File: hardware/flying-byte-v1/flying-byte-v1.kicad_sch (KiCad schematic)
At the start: 44 parts, among them J1 Conn_Coaxial, J2 Conn_ARM_SWD_TagConnect_TC2030, J3 USB_C_Receptacle_USB2.0, J4 Conn_01x04, SW1 SW_Push, U1 STM32WB55CEU6, U2 USBLC6-2SC6_MOD, U3 MIC5365-3.3YD5, X1 32MHz, X2 32kHz768

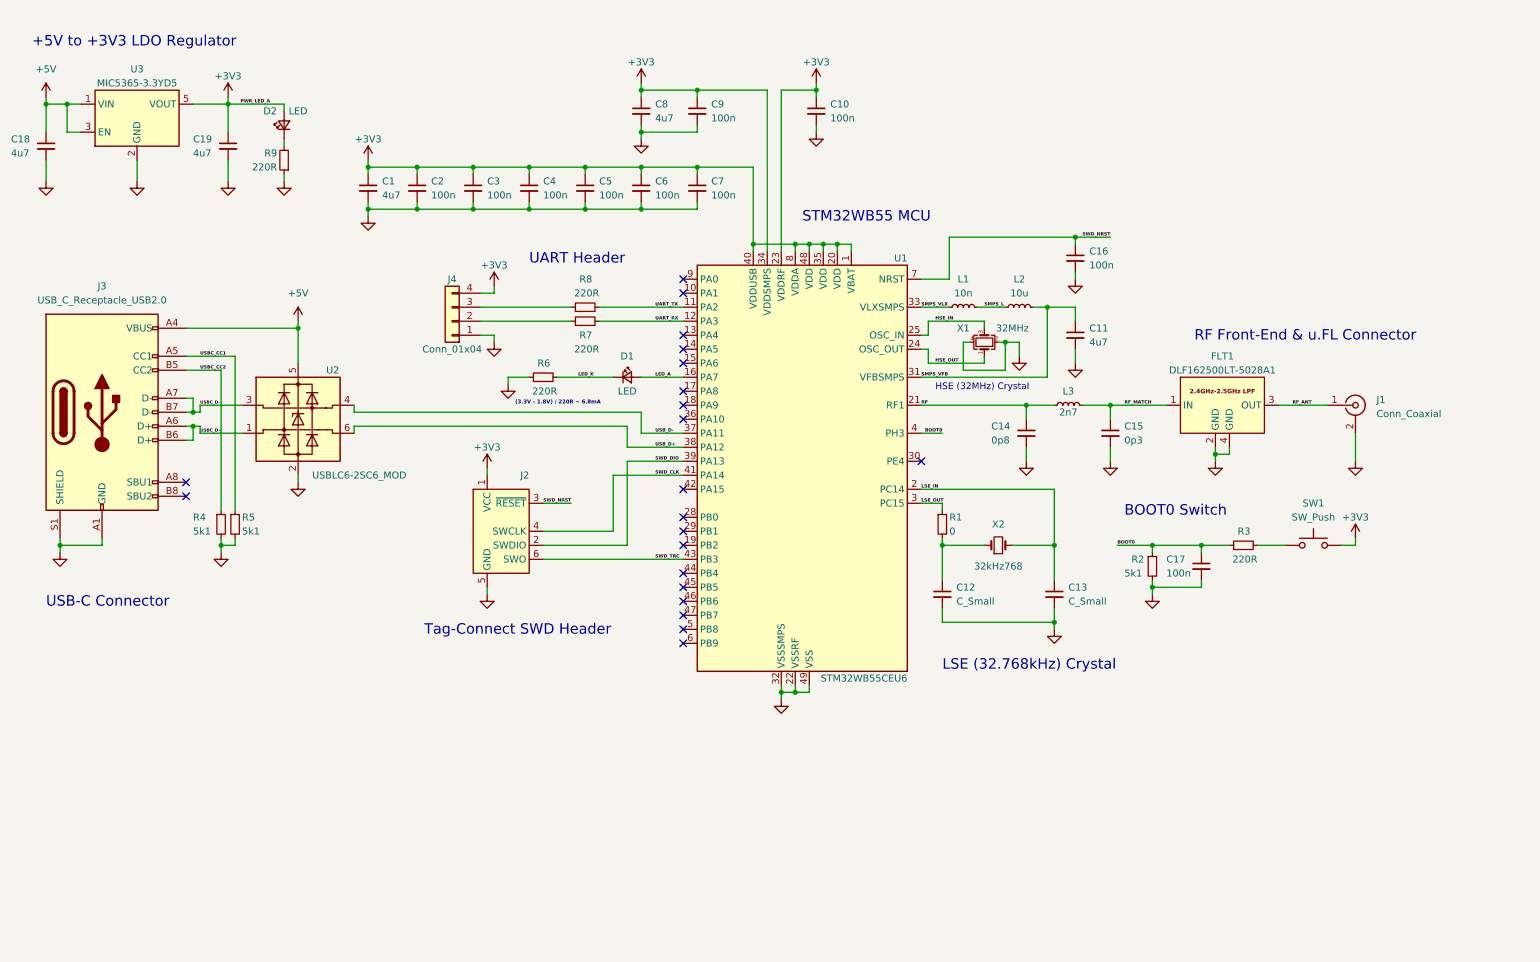
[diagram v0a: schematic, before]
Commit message: feature: Assign footprints after ERC
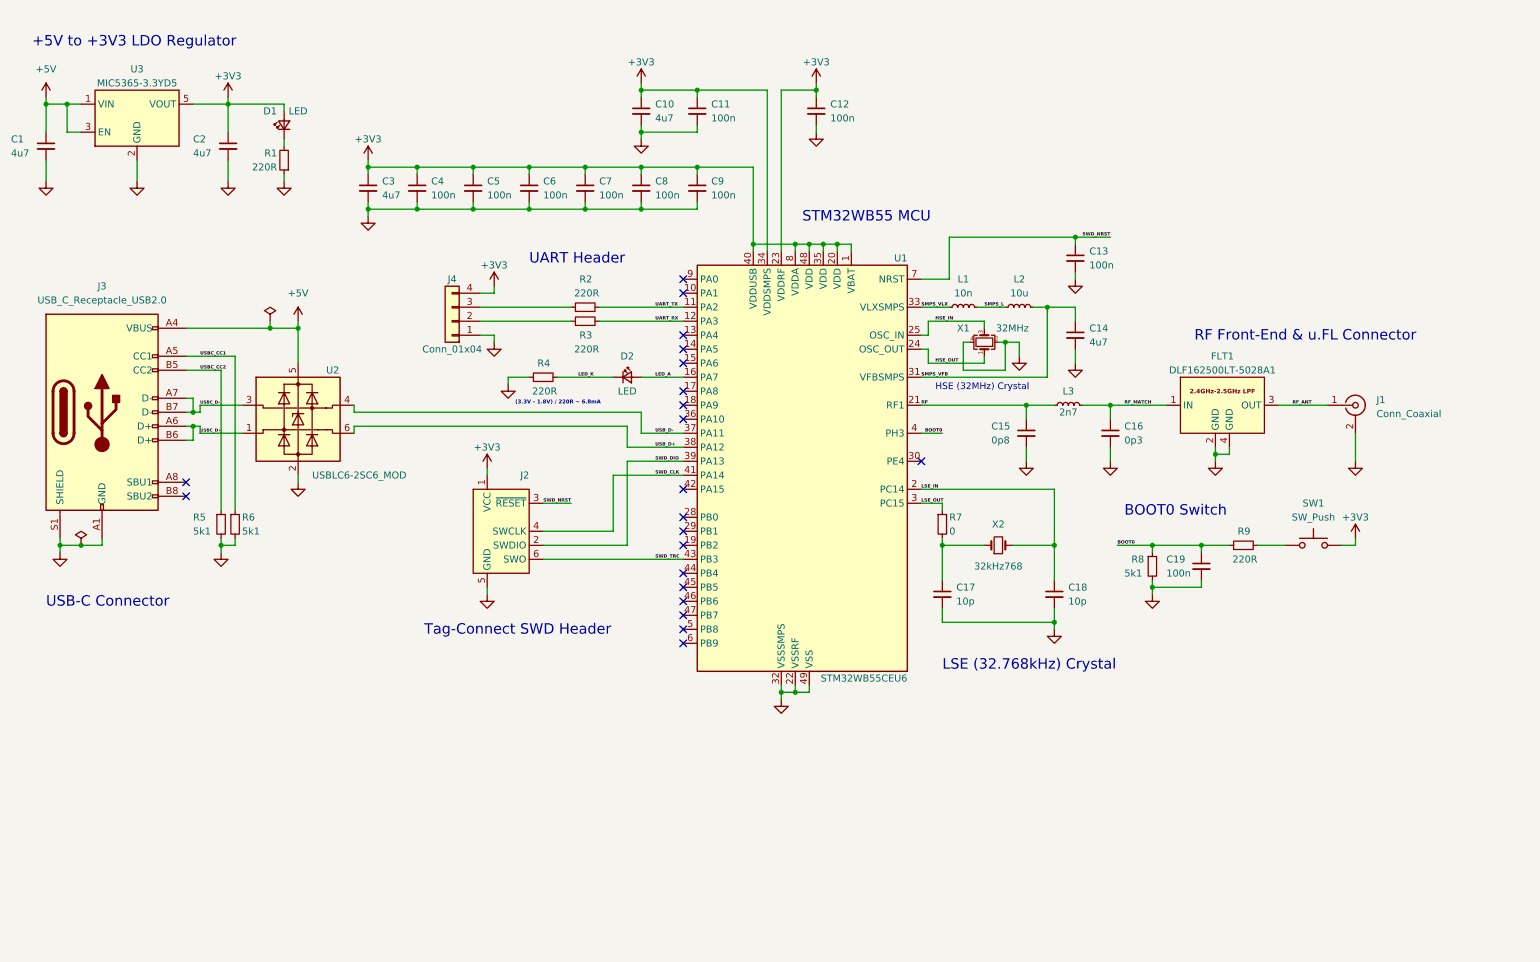
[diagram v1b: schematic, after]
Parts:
- C1: renamed from C18; footprint (none) -> Capacitor_SMD:C_0603_1608Metric; Distribution Link (none) -> https://eu.mouser.com/ProductDetail/Murata-Electronics/GRT1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; Manufacturer Part Number (none) -> GRT188R61E475KE13D; Manufaturer (none) -> Murata Electronics
- C10: renamed from C8; footprint (none) -> Capacitor_SMD:C_0603_1608Metric; Distribution Link (none) -> https://eu.mouser.com/ProductDetail/Murata-Electronics/GRT1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; Manufacturer Part Number (none) -> GRT188R61E475KE13D; Manufaturer (none) -> Murata Electronics
- C11: renamed from C9; footprint (none) -> Capacitor_SMD:C_0402_1005Metric; Distribution Link (none) -> https://eu.mouser.com/ProductDetail/Wurth-Elektronik/885012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; Manufacturer Part Number (none) -> 885012205092; Manufaturer (none) -> Wurth Elektronik
- C12: renamed from C10; footprint (none) -> Capacitor_SMD:C_0402_1005Metric; Distribution Link (none) -> https://eu.mouser.com/ProductDetail/Wurth-Elektronik/885012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; Manufacturer Part Number (none) -> 885012205092; Manufaturer (none) -> Wurth Elektronik
- C13: renamed from C16; footprint (none) -> Capacitor_SMD:C_0402_1005Metric; Distribution Link (none) -> https://eu.mouser.com/ProductDetail/Wurth-Elektronik/885012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; Manufacturer Part Number (none) -> 885012205092; Manufaturer (none) -> Wurth Elektronik
- C14: renamed from C11; footprint (none) -> Capacitor_SMD:C_0603_1608Metric; Distribution Link (none) -> https://eu.mouser.com/ProductDetail/Murata-Electronics/GRT1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; Manufacturer Part Number (none) -> GRT188R61E475KE13D; Manufaturer (none) -> Murata Electronics
- C15: renamed from C14; footprint (none) -> Capacitor_SMD:C_0402_1005Metric; Distribution Link (none) -> https://eu.mouser.com/ProductDetail/Murata-Electronics/GRM1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; Manufacturer Part Number (none) -> GRM1555C1HR80BA01D; Manufaturer (none) -> Murata Electronics
- C16: renamed from C15; footprint (none) -> Capacitor_SMD:C_0402_1005Metric; Distribution Link (none) -> https://eu.mouser.com/ProductDetail/Murata-Electronics/GRM1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; Manufacturer Part Number (none) -> GRM1555C1HR30WA01D; Manufaturer (none) -> Murata Electronics
- C17: renamed from C12; value C_Small -> 10p; footprint (none) -> Capacitor_SMD:C_0402_1005Metric; Distribution Link (none) -> https://eu.mouser.com/ProductDetail/KEMET/C0402C100J5RAC?qs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; Manufacturer Part Number (none) -> C0402C100J5RAC; Manufaturer (none) -> KEMET
- C18: renamed from C13; value C_Small -> 10p; footprint (none) -> Capacitor_SMD:C_0402_1005Metric; Distribution Link (none) -> https://eu.mouser.com/ProductDetail/KEMET/C0402C100J5RAC?qs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; Manufacturer Part Number (none) -> C0402C100J5RAC; Manufaturer (none) -> KEMET
- C19: renamed from C17; footprint (none) -> Capacitor_SMD:C_0402_1005Metric; Distribution Link (none) -> https://eu.mouser.com/ProductDetail/Wurth-Elektronik/885012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; Manufacturer Part Number (none) -> 885012205092; Manufaturer (none) -> Wurth Elektronik
- C2: renamed from C19; footprint (none) -> Capacitor_SMD:C_0603_1608Metric; Distribution Link (none) -> https://eu.mouser.com/ProductDetail/Murata-Electronics/GRT1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; Manufacturer Part Number (none) -> GRT188R61E475KE13D; Manufaturer (none) -> Murata Electronics
- C3: renamed from C1; footprint (none) -> Capacitor_SMD:C_0603_1608Metric; Distribution Link (none) -> https://eu.mouser.com/ProductDetail/Murata-Electronics/GRT1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; Manufacturer Part Number (none) -> GRT188R61E475KE13D; Manufaturer (none) -> Murata Electronics
- C4: renamed from C2; footprint (none) -> Capacitor_SMD:C_0402_1005Metric; Distribution Link (none) -> https://eu.mouser.com/ProductDetail/Wurth-Elektronik/885012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; Manufacturer Part Number (none) -> 885012205092; Manufaturer (none) -> Wurth Elektronik
- C5: renamed from C3; footprint (none) -> Capacitor_SMD:C_0402_1005Metric; Distribution Link (none) -> https://eu.mouser.com/ProductDetail/Wurth-Elektronik/885012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; Manufacturer Part Number (none) -> 885012205092; Manufaturer (none) -> Wurth Elektronik
- C6: renamed from C4; footprint (none) -> Capacitor_SMD:C_0402_1005Metric; Distribution Link (none) -> https://eu.mouser.com/ProductDetail/Wurth-Elektronik/885012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; Manufacturer Part Number (none) -> 885012205092; Manufaturer (none) -> Wurth Elektronik
- C7: renamed from C5; footprint (none) -> Capacitor_SMD:C_0402_1005Metric; Distribution Link (none) -> https://eu.mouser.com/ProductDetail/Wurth-Elektronik/885012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; Manufacturer Part Number (none) -> 885012205092; Manufaturer (none) -> Wurth Elektronik
- C8: renamed from C6; footprint (none) -> Capacitor_SMD:C_0402_1005Metric; Distribution Link (none) -> https://eu.mouser.com/ProductDetail/Wurth-Elektronik/885012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; Manufacturer Part Number (none) -> 885012205092; Manufaturer (none) -> Wurth Elektronik
- C9: renamed from C7; footprint (none) -> Capacitor_SMD:C_0402_1005Metric; Distribution Link (none) -> https://eu.mouser.com/ProductDetail/Wurth-Elektronik/885012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; Manufacturer Part Number (none) -> 885012205092; Manufaturer (none) -> Wurth Elektronik
- D1: renamed from D2; footprint (none) -> LED_SMD:LED_0402_1005Metric; Distribution Link (none) -> https://eu.mouser.com/ProductDetail/Stanley-Electric/FHR110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; Manufacturer Part Number (none) -> FHR1105P-TR; Manufaturer (none) -> Stanley Electric
- D2: renamed from D1; footprint (none) -> LED_SMD:LED_0402_1005Metric; Distribution Link (none) -> https://eu.mouser.com/ProductDetail/Stanley-Electric/FHY110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; Manufacturer Part Number (none) -> FHY1105P-TR; Manufaturer (none) -> Stanley Electric
- FLT1: Distribution Link (none) -> https://eu.mouser.com/ProductDetail/TDK/DLF162500LT-5028A1?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; Manufacturer Part Number (none) -> DLF162500LT-5028A1; Manufaturer (none) -> TDK
- J1: footprint (none) -> Connector_Coaxial:U.FL_Hirose_U.FL-R-SMT-1_Vertical; Distribution Link (none) -> https://eu.mouser.com/ProductDetail/Hirose-Connector/U.FL-R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; Manufacturer Part Number (none) -> U.FL-R-SMT(01); Manufaturer (none) -> Hirose Connector
- J3: footprint (none) -> Connector_USB:USB_C_Receptacle_GCT_USB4105-xx-A_16P_TopMnt_Horizontal; Distribution Link (none) -> https://eu.mouser.com/ProductDetail/GCT/USB4105-GF-A?qs=KUo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; Manufacturer Part Number (none) -> USB4105-GF-A; Manufaturer (none) -> GCT
- J4: footprint (none) -> Connector_Molex:Molex_PicoBlade_53047-0410_1x04_P1.25mm_Vertical; Distribution Link (none) -> https://eu.mouser.com/ProductDetail/Molex/53048-0410?qs=359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; Manufacturer Part Number (none) -> 53048-0410; Manufaturer (none) -> Molex
- L1: footprint (none) -> Inductor_SMD:L_0402_1005Metric; Distribution Link (none) -> https://eu.mouser.com/ProductDetail/Murata-Electronics/LQG1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; Manufacturer Part Number (none) -> LQG15WZ10NJ02D; Manufaturer (none) -> Murata Electronics
- L2: footprint (none) -> Inductor_SMD:L_0805_2012Metric; Distribution Link (none) -> https://eu.mouser.com/ProductDetail/Murata-Electronics/LQM2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; Manufacturer Part Number (none) -> LQM21FN100M80L; Manufaturer (none) -> Murata Electronics
- L3: footprint (none) -> Inductor_SMD:L_0402_1005Metric; Distribution Link (none) -> https://eu.mouser.com/ProductDetail/Murata-Electronics/LQG1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; Manufacturer Part Number (none) -> LQG15HS2N7S02D; Manufaturer (none) -> Murata Electronics
- R1: renamed from R9; footprint (none) -> Resistor_SMD:R_0402_1005Metric; Distribution Link (none) -> https://eu.mouser.com/ProductDetail/SEI-Stackpole/RNCF0402B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; Manufacturer Part Number (none) -> RNCF0402BKE220R; Manufaturer (none) -> SEI Stackpole
- R2: renamed from R8; footprint (none) -> Resistor_SMD:R_0402_1005Metric; Distribution Link (none) -> https://eu.mouser.com/ProductDetail/SEI-Stackpole/RNCF0402B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; Manufacturer Part Number (none) -> RNCF0402BKE220R; Manufaturer (none) -> SEI Stackpole
- R3: renamed from R7; footprint (none) -> Resistor_SMD:R_0402_1005Metric; Distribution Link (none) -> https://eu.mouser.com/ProductDetail/SEI-Stackpole/RNCF0402B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; Manufacturer Part Number (none) -> RNCF0402BKE220R; Manufaturer (none) -> SEI Stackpole
- R4: renamed from R6; footprint (none) -> Resistor_SMD:R_0402_1005Metric; Distribution Link (none) -> https://eu.mouser.com/ProductDetail/SEI-Stackpole/RNCF0402B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; Manufacturer Part Number (none) -> RNCF0402BKE220R; Manufaturer (none) -> SEI Stackpole
- R5: renamed from R4; footprint (none) -> Resistor_SMD:R_0402_1005Metric; Distribution Link (none) -> https://eu.mouser.com/ProductDetail/SEI-Stackpole/RNCF0402B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; Manufacturer Part Number (none) -> RNCF0402BKE5K10; Manufaturer (none) -> SEI Stackpole
- R6: renamed from R5; footprint (none) -> Resistor_SMD:R_0402_1005Metric; Distribution Link (none) -> https://eu.mouser.com/ProductDetail/SEI-Stackpole/RNCF0402B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; Manufacturer Part Number (none) -> RNCF0402BKE5K10; Manufaturer (none) -> SEI Stackpole
- R7: renamed from R1; footprint (none) -> Resistor_SMD:R_0402_1005Metric; Distribution Link (none) -> https://eu.mouser.com/ProductDetail/Vishay-Beyschlag/MCS040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; Manufacturer Part Number (none) -> MCS04020Z0000ZE000; Manufaturer (none) -> Vishay / Beyschlag
- R8: renamed from R2; footprint (none) -> Resistor_SMD:R_0402_1005Metric; Distribution Link (none) -> https://eu.mouser.com/ProductDetail/SEI-Stackpole/RNCF0402B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; Manufacturer Part Number (none) -> RNCF0402BKE5K10; Manufaturer (none) -> SEI Stackpole
- R9: renamed from R3; footprint (none) -> Resistor_SMD:R_0402_1005Metric; Distribution Link (none) -> https://eu.mouser.com/ProductDetail/SEI-Stackpole/RNCF0402B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; Manufacturer Part Number (none) -> RNCF0402BKE220R; Manufaturer (none) -> SEI Stackpole
- SW1: footprint (none) -> Button_Switch_SMD:SW_SPST_CK_RS282G05A3; Distribution Link (none) -> https://eu.mouser.com/ProductDetail/CK/RS282G05A3SMRT?qs=Gu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; Manufacturer Part Number (none) -> RS282G05A3SMRT; Manufaturer (none) -> C&K
- U1: Distribution Link (none) -> https://eu.mouser.com/ProductDetail/STMicroelectronics/STM3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; Manufacturer Part Number (none) -> STM32WB55CEU6; Manufaturer (none) -> STMicroelectronics
- U2: Distribution Link (none) -> https://eu.mouser.com/ProductDetail/STMicroelectronics/USBL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; Manufacturer Part Number (none) -> USBLC6-2SC6; Manufaturer (none) -> STMicroelectronics
- U3: Distribution Link (none) -> https://eu.mouser.com/ProductDetail/Microchip-Technology/MI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; Manufacturer Part Number (none) -> MIC5365-3.3YD5-TR; Manufaturer (none) -> Microchip Technology
- X1: footprint (none) -> Crystal:Crystal_SMD_2016-4Pin_2.0x1.6mm; Distribution Link (none) -> https://eu.mouser.com/ProductDetail/NDK/NX2016SA-32M-EXS00A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; Manufacturer Part Number (none) -> NX2016SA-32M-EXS00A-CS06465; Manufaturer (none) -> NDK
- X2: footprint (none) -> Crystal:Crystal_SMD_2012-2Pin_2.0x1.2mm; Distribution Link (none) -> https://eu.mouser.com/ProductDetail/NDK/NX2012SA-32.768K-ST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; Manufacturer Part Number (none) -> NX2012SA-32.768K-STD-MUB-1; Manufaturer (none) -> NDK

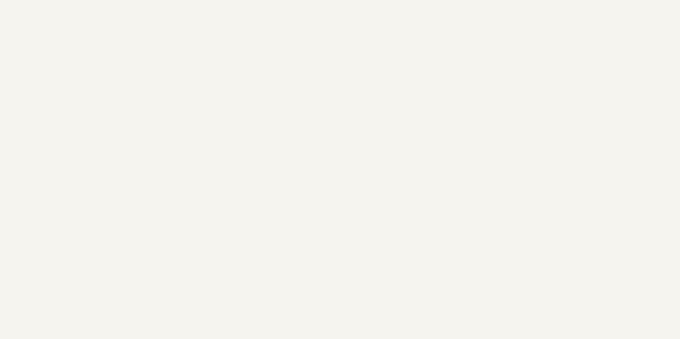
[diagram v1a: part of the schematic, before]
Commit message: doc: Add the page settings
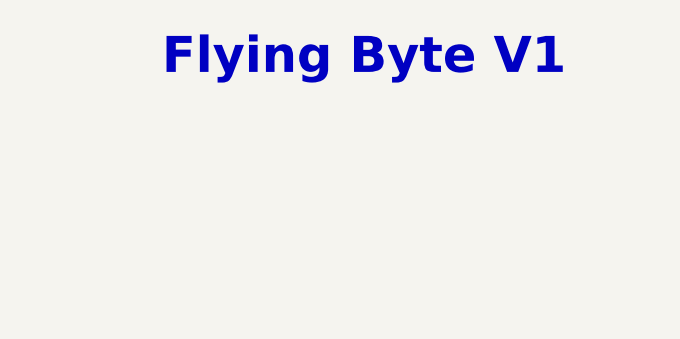
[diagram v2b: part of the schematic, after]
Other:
- note added: "Flying Byte V1"
- title: (none) -> Flying Byte
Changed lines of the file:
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@@
 (kicad_sch (version 20230121) (generator eeschema)
   (paper "A4")
+  (title_block
+    (title "Flying Byte")
+    (date "2025-03-06")
+    (rev "1.0")
+    (comment 1 "The flying byte prototype v1")
+  )
   (junction (at 29.21 111.76) (diameter 0) (color 0 0 0 0)
   )
@@
     (stroke (width 0) (type default))
   )
+  (text "Flying Byte V1" (at 236.22 21.59 0)
+    (effects (font (size 4 4) (thickness 0.8) bold) (justify left bottom))
+  )
   (text "RF Front-End & u.FL Connector" (at 231.14 74.93 0)

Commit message: feat: Add the initial layout
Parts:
- J4: footprint Connector_Molex:Molex_PicoBlade_53047-0410_1x04_P1.25mm_Vertical -> Connector_Molex:Molex_PicoBlade_53048-0410_1x04_P1.25mm_Horizontal
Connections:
- net LSE_OUT_R: now reaches C17.1, R7.2, X2.1
- net BOOT0_SW: now reaches R9.2, SW1.1
- net UART_TXC: now reaches J4.3 (Pin_3), R2.1
- net UART_RXC: now reaches J4.2 (Pin_2), R3.1
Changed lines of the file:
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@@
+    (effects (font (size 0.6 0.6) (thickness 0.21) bold) (justify left bottom))
+  )
+  (label "BOOT0_SW" (at 243.84 111.76 0) (fields_autoplaced)
     (effects (font (size 0.6 0.6) (thickness 0.21) bold) (justify left bottom))
   )
@@
     (effects (font (size 0.6 0.6) (thickness 0.21) bold) (justify right bottom))
   )
+  (label "UART_RXC" (at 102.87 71.12 0) (fields_autoplaced)
+    (effects (font (size 0.6 0.6) (thickness 0.21) bold) (justify left bottom))
+  )
   (label "SMPS_VLX" (at 181.61 68.58 0) (fields_autoplaced)
     (effects (font (size 0.6 0.6) (thickness 0.21) bold) (justify left bottom))
   )
+  (label "LSE_OUT_R" (at 186.69 111.76 0) (fields_autoplaced)
+    (effects (font (size 0.6 0.6) (thickness 0.21) bold) (justify left bottom))
+  )
   (label "UART_RX" (at 133.35 71.12 0) (fields_autoplaced)
+    (effects (font (size 0.6 0.6) (thickness 0.21) bold) (justify left bottom))
+  )
+  (label "UART_TXC" (at 102.87 68.58 0) (fields_autoplaced)
     (effects (font (size 0.6 0.6) (thickness 0.21) bold) (justify left bottom))
   )
@@
       (effects (font (size 1.27 1.27)))
     )
-    (property "Footprint" "Connector_Molex:Molex_PicoBlade_53047-0410_1x04_P1.25mm_Vertical" (at 96.52 71.12 0)
-      (effects (font (size 1.27 1.27)) hide)
-    )
+    (property "Footprint" "Connector_Molex:Molex_PicoBlade_53048-0410_1x04_P1.25mm_Horizontal" (at 96.52 71.12 0)
+      (effects (font (size 1.27 1.27)) hide)
+    )

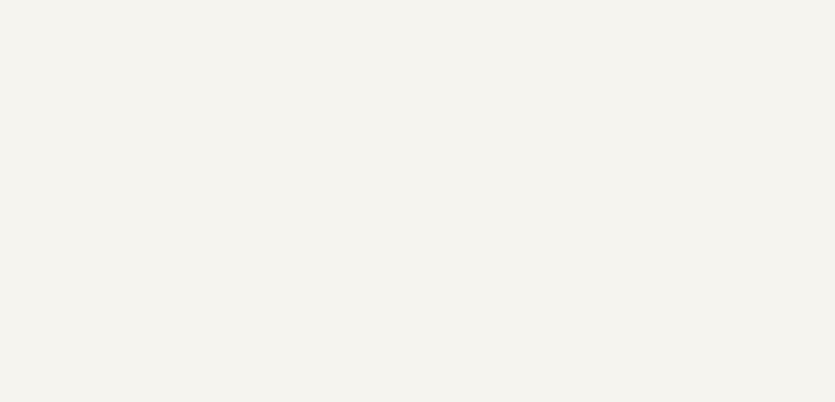
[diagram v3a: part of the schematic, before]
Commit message: feat: Add outline, mounting holes and fiducial markers
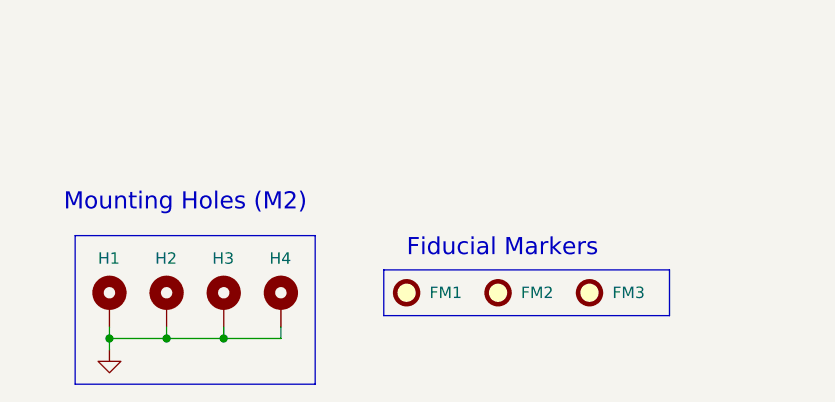
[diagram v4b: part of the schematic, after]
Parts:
- added FM1, FM2, FM3: Fiducial, Fiducial:Fiducial_1mm_Mask2mm, symbol Mechanical:Fiducial
- added H1, H2, H3, H4: MountingHole_Pad, MountingHole:MountingHole_2.2mm_M2_Pad, symbol Mechanical:MountingHole_Pad
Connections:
- net GND: now also H1.1, H2.1, H3.1, H4.1
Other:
- note added: "Fiducial Markers"
- note added: "Mounting Holes (M2)"

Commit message: feat: PCB routing #2
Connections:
- net USBC_D+: now also U2.3 (I/O1); no longer U2.1 (I/O1)
- net USBC_D-: now also U2.1 (I/O1); no longer U2.3 (I/O1)
- net USB_D+: now also U2.4 (I/O2); no longer U2.6 (I/O2)
- net USB_D-: now also U2.6 (I/O2); no longer U2.4 (I/O2)
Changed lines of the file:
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@@
       (effects (font (size 1.27 1.27)) hide)
     )
+    (pin "3")
+    (pin "2")
     (pin "1")
-    (pin "2")
-    (pin "3")
+    (pin "6")
+    (pin "5")
     (pin "4")
-    (pin "5")
-    (pin "6")
     (instances
       (project "flying-byte-v1"
